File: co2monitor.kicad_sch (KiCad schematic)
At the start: 43 parts, among them J1 USB_C_Receptacle_USB2.0, J2 UART, J3 I2C, J4 5V, SW1 RESET, SW2 BOOT, U1 AP2112K-3.3, U2 ESP32-S3-WROOM-1, U3 BME680, U4 SCD40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

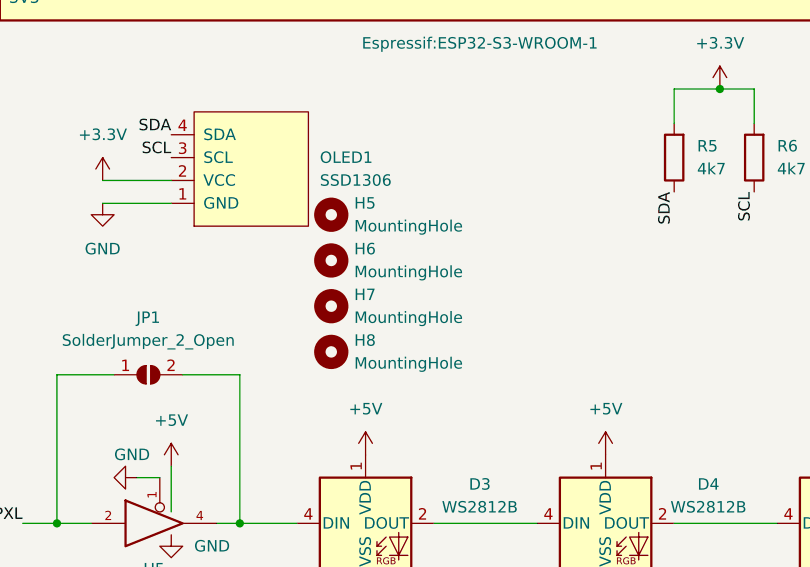
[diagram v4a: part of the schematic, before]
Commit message: use the mounting holes in the footprint
We don't need to duplicate these ourselves!
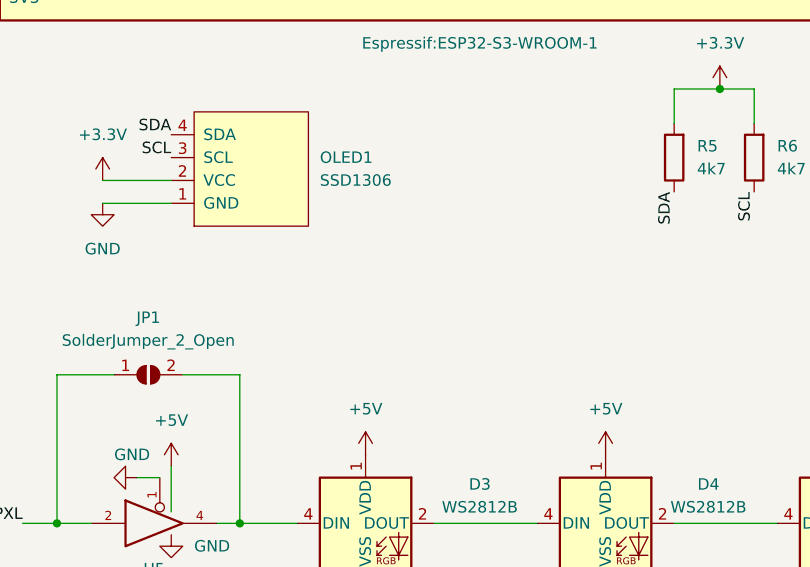
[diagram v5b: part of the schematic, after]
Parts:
- removed H5, H6, H7, H8: MountingHole, MountingHole:MountingHole_2.7mm, symbol Mechanical:MountingHole
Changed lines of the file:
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@@
-    )
-  )
-  (symbol (lib_id "Mechanical:MountingHole") (at 201.93 116.84 0) (unit 1)
-    (in_bom yes) (on_board yes) (fields_autoplaced)
-    (property "Reference" "H7" (id 0) (at 204.47 115.5699 0)
-      (effects (font (size 1.27 1.27)) (justify left))
-    )
-    (property "Value" "MountingHole" (id 1) (at 204.47 118.1099 0)
-      (effects (font (size 1.27 1.27)) (justify left))
-    )
-    (property "Footprint" "MountingHole:MountingHole_2.7mm" (id 2) (at 201.93 116.84 0)
-      (effects (font (size 1.27 1.27)) hide)
-    )
-    (property "Datasheet" "~" (id 3) (at 201.93 116.84 0)
-      (effects (font (size 1.27 1.27)) hide)
     )
   )
@@
     (pin "1")
   )
-  (symbol (lib_id "Mechanical:MountingHole") (at 201.93 111.76 0) (unit 1)
-    (in_bom yes) (on_board yes) (fields_autoplaced)
-    (property "Reference" "H6" (id 0) (at 204.47 110.4899 0)
-      (effects (font (size 1.27 1.27)) (justify left))
-    )
-    (property "Value" "MountingHole" (id 1) (at 204.47 113.0299 0)
-      (effects (font (size 1.27 1.27)) (justify left))
-    )
-    (property "Footprint" "MountingHole:MountingHole_2.7mm" (id 2) (at 201.93 111.76 0)
-      (effects (font (size 1.27 1.27)) hide)
-    )
-    (property "Datasheet" "~" (id 3) (at 201.93 111.76 0)
-      (effects (font (size 1.27 1.27)) hide)
-    )
-  )
   (symbol (lib_id "power:GND") (at 205.74 148.59 0) (unit 1)
     (in_bom yes) (on_board yes) (fields_autoplaced)
@@
     )
     (pin "1")
-  )
-  (symbol (lib_id "Mechanical:MountingHole") (at 201.93 121.92 0) (unit 1)
-    (in_bom yes) (on_board yes) (fields_autoplaced)
-    (property "Reference" "H8" (id 0) (at 204.47 120.6499 0)
-      (effects (font (size 1.27 1.27)) (justify left))
-    )
-    (property "Value" "MountingHole" (id 1) (at 204.47 123.1899 0)
-      (effects (font (size 1.27 1.27)) (justify left))
-    )
-    (property "Footprint" "MountingHole:MountingHole_2.7mm" (id 2) (at 201.93 121.92 0)
-      (effects (font (size 1.27 1.27)) hide)
-    )
-    (property "Datasheet" "~" (id 3) (at 201.93 121.92 0)
-      (effects (font (size 1.27 1.27)) hide)
-    )
   )
   (symbol (lib_id "Device:C") (at 110.49 62.23 270) (unit 1)
@@
     (pin "1")
     (pin "2")
-  )
-  (symbol (lib_id "Mechanical:MountingHole") (at 201.93 106.68 0) (unit 1)
-    (in_bom yes) (on_board yes) (fields_autoplaced)
-    (property "Reference" "H5" (id 0) (at 204.47 105.4099 0)
-      (effects (font (size 1.27 1.27)) (justify left))
-    )
-    (property "Value" "MountingHole" (id 1) (at 204.47 107.9499 0)
-      (effects (font (size 1.27 1.27)) (justify left))
-    )
-    (property "Footprint" "MountingHole:MountingHole_2.7mm" (id 2) (at 201.93 106.68 0)
-      (effects (font (size 1.27 1.27)) hide)
-    )
-    (property "Datasheet" "~" (id 3) (at 201.93 106.68 0)
-      (effects (font (size 1.27 1.27)) hide)
-    )
   )
   (symbol (lib_id "power:GND") (at 53.34 31.75 0) (unit 1)
@@
       (reference "H4") (unit 1) (value "MountingHole") (footprint "MountingHole:MountingHole_3.5mm")
     )
-    (path "/a3daf831-6b2f-4c2d-a1a8-61b0f1635f5c"
-      (reference "H5") (unit 1) (value "MountingHole") (footprint "MountingHole:MountingHole_2.7mm")
-    )
-    (path "/9838bd47-1c23-4649-b7ae-c2930116a0bb"
-      (reference "H6") (unit 1) (value "MountingHole") (footprint "MountingHole:MountingHole_2.7mm")
-    )
-    (path "/4a315ce3-6e1e-44fd-b749-311f9a63d813"
-      (reference "H7") (unit 1) (value "MountingHole") (footprint "MountingHole:MountingHole_2.7mm")
-    )
-    (path "/a1fa586c-885e-4bcb-a564-7b2a804264af"
-      (reference "H8") (unit 1) (value "MountingHole") (footprint "MountingHole:MountingHole_2.7mm")
-    )
     (path "/abbd7cc5-9fa9-42ab-af2d-72d337980e6e"

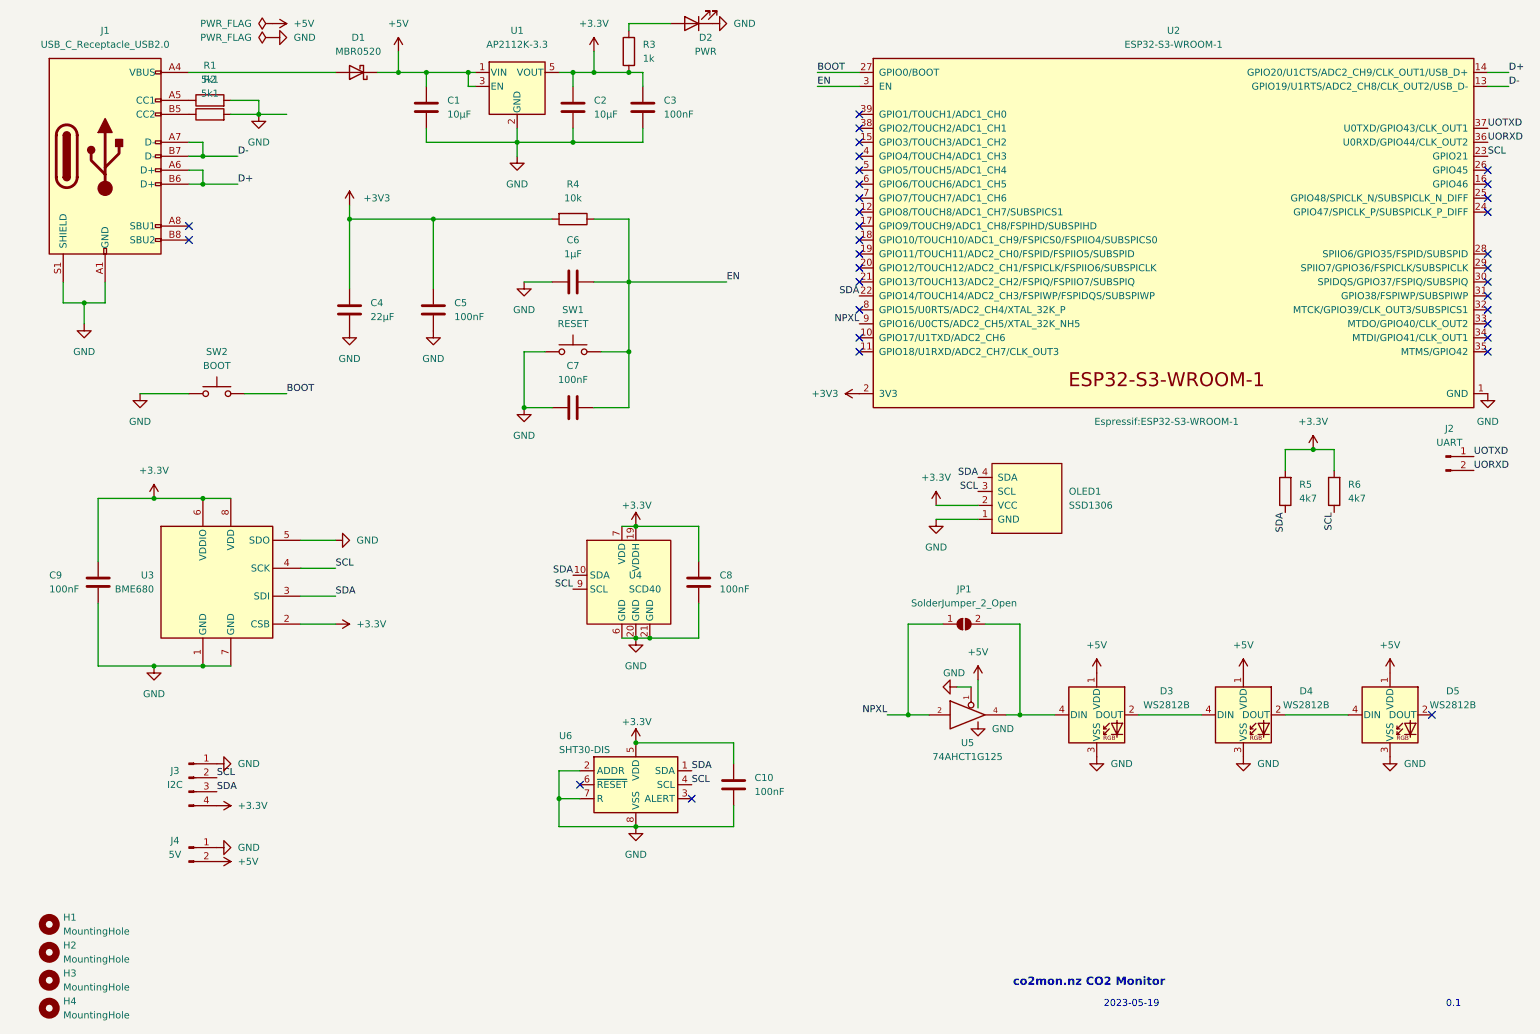
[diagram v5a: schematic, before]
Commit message: Add JTAG header
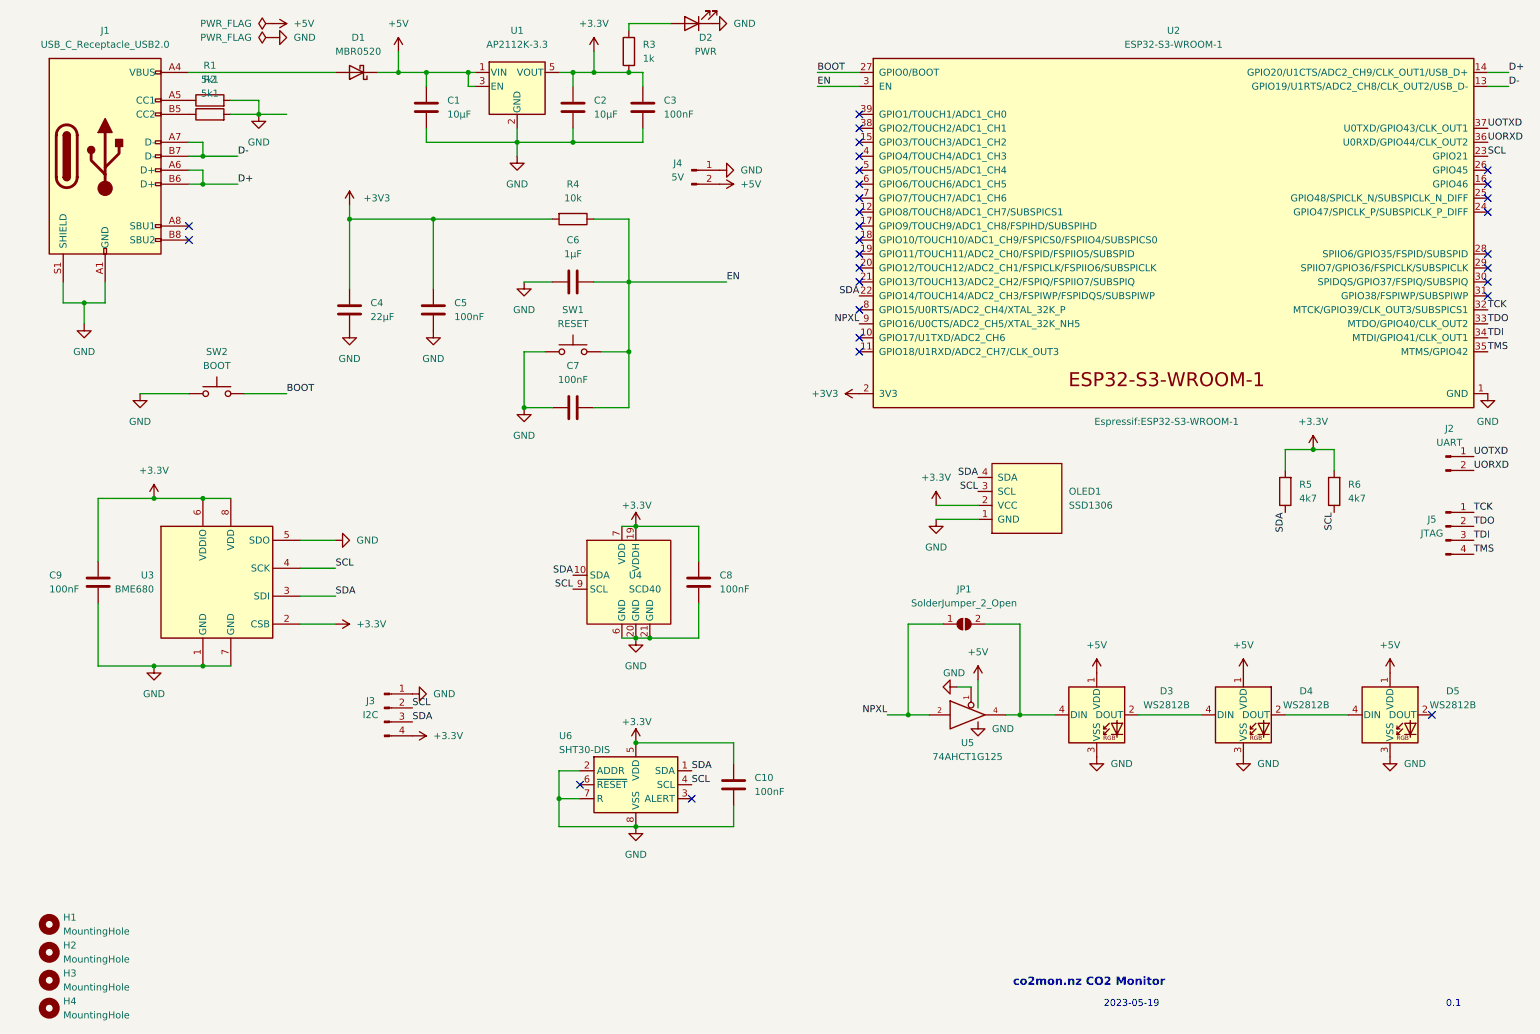
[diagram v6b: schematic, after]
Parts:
- added J5: JTAG, Connector_PinHeader_2.00mm:PinHeader_1x04_P2.00mm_Vertical, symbol Connector:Conn_01x04_Male
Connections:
- net TCK: now reaches U2.32 (MTCK/GPIO39/CLK_OUT3/SUBSPICS1)
- net TCK: now also J5.1 (Pin_1)
- net TDO: now reaches U2.33 (MTDO/GPIO40/CLK_OUT2)
- net TDO: now also J5.2 (Pin_2)
- net TDI: now reaches U2.34 (MTDI/GPIO41/CLK_OUT1)
- net TDI: now also J5.3 (Pin_3)
- net TMS: now reaches U2.35 (MTMS/GPIO42)
- net TMS: now also J5.4 (Pin_4)
- no-connect marks 33 -> 29
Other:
- moved on the sheet: J3, J4
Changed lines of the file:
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@@
   (no_connect (at 162.56 62.23))
   (no_connect (at 162.56 41.91))
-  (no_connect (at 276.86 72.39))
   (no_connect (at 276.86 41.91))
   (no_connect (at 40.64 52.07))
-  (no_connect (at 276.86 74.93))
   (no_connect (at 162.56 34.29))
-  (no_connect (at 276.86 69.85))
   (no_connect (at 111.76 153.67))
   (no_connect (at 276.86 44.45))
@@
   (no_connect (at 276.86 62.23))
   (no_connect (at 276.86 64.77))
-  (no_connect (at 276.86 67.31))
   (no_connect (at 162.56 59.69))
   (no_connect (at 276.86 57.15))
@@
     (effects (font (size 1.27 1.27)) (justify left bottom))
   )
+  (label "TCK" (at 274.32 104.14 0)
+    (effects (font (size 1.27 1.27)) (justify left bottom))
+  )
   (label "SDA" (at 132.08 151.13 0)
     (effects (font (size 1.27 1.27)) (justify left bottom))
@@
     (effects (font (size 1.27 1.27)) (justify left bottom))
   )
-  (label "SDA" (at 45.72 154.94 0)
+  (label "SDA" (at 81.28 142.24 0)
+    (effects (font (size 1.27 1.27)) (justify left bottom))
+  )
+  (label "TDI" (at 276.86 72.39 0)
+    (effects (font (size 1.27 1.27)) (justify left bottom))
+  )
+  (label "TDO" (at 274.32 106.68 0)
     (effects (font (size 1.27 1.27)) (justify left bottom))
   )
@@
     (effects (font (size 1.27 1.27)) (justify left bottom))
   )
+  (label "TMS" (at 276.86 74.93 0)
+    (effects (font (size 1.27 1.27)) (justify left bottom))
+  )
   (label "SDA" (at 240.03 104.14 270)
     (effects (font (size 1.27 1.27)) (justify right bottom))
@@
     (effects (font (size 1.27 1.27)) (justify left bottom))
   )
-  (label "SCL" (at 45.72 152.4 0)
+  (label "TDI" (at 274.32 109.22 0)
+    (effects (font (size 1.27 1.27)) (justify left bottom))
+  )
+  (label "SCL" (at 81.28 139.7 0)
     (effects (font (size 1.27 1.27)) (justify left bottom))
   )
@@
     (effects (font (size 1.27 1.27)) (justify left bottom))
   )
+  (label "TCK" (at 276.86 67.31 0)
+    (effects (font (size 1.27 1.27)) (justify left bottom))
+  )
   (label "SCL" (at 132.08 153.67 0)
     (effects (font (size 1.27 1.27)) (justify left bottom))
@@
   )
   (label "D-" (at 280.67 26.67 0)
+    (effects (font (size 1.27 1.27)) (justify left bottom))
+  )
+  (label "TMS" (at 274.32 111.76 0)
     (effects (font (size 1.27 1.27)) (justify left bottom))
   )
   (label "SCL" (at 184.15 100.33 180)
     (effects (font (size 1.27 1.27)) (justify right bottom))
+  )
+  (label "TDO" (at 276.86 69.85 0)
+    (effects (font (size 1.27 1.27)) (justify left bottom))
   )
   (symbol (lib_id "power:GND") (at 21.59 69.85 0) (unit 1)
@@
     (pin "2")
   )
-  (symbol (lib_id "Connector:Conn_01x04_Male") (at 40.64 152.4 0) (unit 1)
+  (symbol (lib_id "Connector:Conn_01x04_Male") (at 76.2 139.7 0) (unit 1)
     (in_bom yes) (on_board yes)
-    (property "Reference" "J3" (id 0) (at 38.1 151.13 0))
-    (property "Value" "I2C" (id 1) (at 38.1 153.67 0))
-    (property "Footprint" "Connector_PinHeader_2.00mm:PinHeader_1x04_P2.00mm_Vertical" (id 2) (at 40.64 152.4 0)
-      (effects (font (size 1.27 1.27)) hide)
-    )
-    (property "Datasheet" "~" (id 3) (at 40.64 152.4 0)
+    (property "Reference" "J3" (id 0) (at 73.66 138.43 0))
+    (property "Value" "I2C" (id 1) (at 73.66 140.97 0))
+    (property "Footprint" "Connector_PinHeader_2.00mm:PinHeader_1x04_P2.00mm_Vertical" (id 2) (at 76.2 139.7 0)
+      (effects (font (size 1.27 1.27)) hide)
+    )
+    (property "Datasheet" "~" (id 3) (at 76.2 139.7 0)
       (effects (font (size 1.27 1.27)) hide)
     )
@@
     (pin "1")
   )
-  (symbol (lib_id "power:GND") (at 45.72 165.1 90) (unit 1)
-    (in_bom yes) (on_board yes) (fields_autoplaced)
-    (property "Reference" "#PWR0120" (id 0) (at 52.07 165.1 0)
-      (effects (font (size 1.27 1.27)) hide)
-    )
-    (property "Value" "GND" (id 1) (at 49.53 165.0999 90)
-      (effects (font (size 1.27 1.27)) (justify right))
-    )
-    (property "Footprint" "" (id 2) (at 45.72 165.1 0)
-      (effects (font (size 1.27 1.27)) hide)
-    )
-    (property "Datasheet" "" (id 3) (at 45.72 165.1 0)
+  (symbol (lib_id "power:GND") (at 137.16 41.91 90) (unit 1)
+    (in_bom yes) (on_board yes) (fields_autoplaced)
+    (property "Reference" "#PWR0120" (id 0) (at 143.51 41.91 0)
+      (effects (font (size 1.27 1.27)) hide)
+    )
+    (property "Value" "GND" (id 1) (at 140.97 41.9099 90)
+      (effects (font (size 1.27 1.27)) (justify right))
+    )
+    (property "Footprint" "" (id 2) (at 137.16 41.91 0)
+      (effects (font (size 1.27 1.27)) hide)
+    )
+    (property "Datasheet" "" (id 3) (at 137.16 41.91 0)
       (effects (font (size 1.27 1.27)) hide)
     )
@@
     (pin "1")
   )
-  (symbol (lib_id "power:+5V") (at 45.72 167.64 270) (unit 1)
-    (in_bom yes) (on_board yes) (fields_autoplaced)
-    (property "Reference" "#PWR0121" (id 0) (at 41.91 167.64 0)
-      (effects (font (size 1.27 1.27)) hide)
-    )
-    (property "Value" "+5V" (id 1) (at 49.53 167.6399 90)
-      (effects (font (size 1.27 1.27)) (justify left))
-    )
-    (property "Footprint" "" (id 2) (at 45.72 167.64 0)
-      (effects (font (size 1.27 1.27)) hide)
-    )
-    (property "Datasheet" "" (id 3) (at 45.72 167.64 0)
+  (symbol (lib_id "power:+5V") (at 137.16 44.45 270) (unit 1)
+    (in_bom yes) (on_board yes) (fields_autoplaced)
+    (property "Reference" "#PWR0121" (id 0) (at 133.35 44.45 0)
+      (effects (font (size 1.27 1.27)) hide)
+    )
+    (property "Value" "+5V" (id 1) (at 140.97 44.4499 90)
+      (effects (font (size 1.27 1.27)) (justify left))
+    )
+    (property "Footprint" "" (id 2) (at 137.16 44.45 0)
+      (effects (font (size 1.27 1.27)) hide)
+    )
+    (property "Datasheet" "" (id 3) (at 137.16 44.45 0)
       (effects (font (size 1.27 1.27)) hide)
     )
@@
     (pin "1")
   )
-  (symbol (lib_id "power:+3.3V") (at 45.72 157.48 270) (unit 1)
-    (in_bom yes) (on_board yes) (fields_autoplaced)
-    (property "Reference" "#PWR019" (id 0) (at 41.91 157.48 0)
-      (effects (font (size 1.27 1.27)) hide)
-    )
-    (property "Value" "+3.3V" (id 1) (at 49.53 157.4799 90)
-      (effects (font (size 1.27 1.27)) (justify left))
-    )
-    (property "Footprint" "" (id 2) (at 45.72 157.48 0)
-      (effects (font (size 1.27 1.27)) hide)
-    )
-    (property "Datasheet" "" (id 3) (at 45.72 157.48 0)
+  (symbol (lib_id "power:+3.3V") (at 81.28 144.78 270) (unit 1)
+    (in_bom yes) (on_board yes) (fields_autoplaced)
+    (property "Reference" "#PWR019" (id 0) (at 77.47 144.78 0)
+      (effects (font (size 1.27 1.27)) hide)
+    )
+    (property "Value" "+3.3V" (id 1) (at 85.09 144.7799 90)
+      (effects (font (size 1.27 1.27)) (justify left))
+    )
+    (property "Footprint" "" (id 2) (at 81.28 144.78 0)
+      (effects (font (size 1.27 1.27)) hide)
+    )
+    (property "Datasheet" "" (id 3) (at 81.28 144.78 0)
       (effects (font (size 1.27 1.27)) hide)
     )
@@
     (pin "1")
   )
+  (symbol (lib_id "Connector:Conn_01x04_Male") (at 269.24 106.68 0) (unit 1)
+    (in_bom yes) (on_board yes)
+    (property "Reference" "J5" (id 0) (at 266.7 105.41 0))
+    (property "Value" "JTAG" (id 1) (at 266.7 107.95 0))
+    (property "Footprint" "Connector_PinHeader_2.00mm:PinHeader_1x04_P2.00mm_Vertical" (id 2) (at 269.24 106.68 0)
+      (effects (font (size 1.27 1.27)) hide)
+    )
+    (property "Datasheet" "~" (id 3) (at 269.24 106.68 0)
+      (effects (font (size 1.27 1.27)) hide)
+    )
+    (pin "1")
+    (pin "2")
+    (pin "3")
+    (pin "4")
+  )
   (symbol (lib_id "Device:R") (at 248.92 100.33 180) (unit 1)
     (in_bom yes) (on_board yes) (fields_autoplaced)
@@
     (pin "2")
   )
-  (symbol (lib_id "Connector:Conn_01x02_Male") (at 40.64 165.1 0) (unit 1)
+  (symbol (lib_id "Connector:Conn_01x02_Male") (at 132.08 41.91 0) (unit 1)
     (in_bom yes) (on_board yes)
-    (property "Reference" "J4" (id 0) (at 38.1 163.83 0))
-    (property "Value" "5V" (id 1) (at 38.1 166.37 0))
-    (property "Footprint" "Connector_PinHeader_2.00mm:PinHeader_1x02_P2.00mm_Vertical" (id 2) (at 40.64 165.1 0)
-      (effects (font (size 1.27 1.27)) hide)
-    )
-    (property "Datasheet" "~" (id 3) (at 40.64 165.1 0)
+    (property "Reference" "J4" (id 0) (at 129.54 40.64 0))
+    (property "Value" "5V" (id 1) (at 129.54 43.18 0))
+    (property "Footprint" "Connector_PinHeader_2.00mm:PinHeader_1x02_P2.00mm_Vertical" (id 2) (at 132.08 41.91 0)
+      (effects (font (size 1.27 1.27)) hide)
+    )
+    (property "Datasheet" "~" (id 3) (at 132.08 41.91 0)
       (effects (font (size 1.27 1.27)) hide)
     )
@@
     (pin "1")
   )
-  (symbol (lib_id "power:GND") (at 45.72 149.86 90) (unit 1)
-    (in_bom yes) (on_board yes) (fields_autoplaced)
-    (property "Reference" "#PWR018" (id 0) (at 52.07 149.86 0)
-      (effects (font (size 1.27 1.27)) hide)
-    )
-    (property "Value" "GND" (id 1) (at 49.53 149.8599 90)
-      (effects (font (size 1.27 1.27)) (justify right))
-    )
-    (property "Footprint" "" (id 2) (at 45.72 149.86 0)
-      (effects (font (size 1.27 1.27)) hide)
-    )
-    (property "Datasheet" "" (id 3) (at 45.72 149.86 0)
+  (symbol (lib_id "power:GND") (at 81.28 137.16 90) (unit 1)
+    (in_bom yes) (on_board yes) (fields_autoplaced)
+    (property "Reference" "#PWR018" (id 0) (at 87.63 137.16 0)
+      (effects (font (size 1.27 1.27)) hide)
+    )
+    (property "Value" "GND" (id 1) (at 85.09 137.1599 90)
+      (effects (font (size 1.27 1.27)) (justify right))
+    )
+    (property "Footprint" "" (id 2) (at 81.28 137.16 0)
+      (effects (font (size 1.27 1.27)) hide)
+    )
+    (property "Datasheet" "" (id 3) (at 81.28 137.16 0)
       (effects (font (size 1.27 1.27)) hide)
     )
@@
       (reference "J4") (unit 1) (value "5V") (footprint "Connector_PinHeader_2.00mm:PinHeader_1x02_P2.00mm_Vertical")
     )
+    (path "/b5eda257-b465-4b2b-ad1b-8198f7d79cc8"
+      (reference "J5") (unit 1) (value "JTAG") (footprint "Connector_PinHeader_2.00mm:PinHeader_1x04_P2.00mm_Vertical")
+    )
     (path "/60713cde-8e76-4e1c-8936-08484f92c4ae"
